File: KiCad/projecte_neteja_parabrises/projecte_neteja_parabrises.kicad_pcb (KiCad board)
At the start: 2 copper layers, 106.5 x 95.3 mm, 77 parts, among them J1 Conn_01x05_Pin, J2 DE9_Pins, J3 DE9_Pins, J4 Conn_01x02_Pin, K2 Fujitsu_FTR-LYAA005x, K3 Fujitsu_FTR-LYAA005x, K4 Fujitsu_FTR-LYAA005x, M1 Motor_DC, M2 Motor_DC, M3 Motor_DC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

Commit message: pcb
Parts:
- added TP1: TestPoint, TestPoint:TestPoint_Keystone_5015_Micro_Mini, F.Cu at (209.1, 109.7)
- added TP2: TestPoint, TestPoint:TestPoint_Keystone_5015_Micro_Mini, F.Cu at (209.1, 114.0)
- added TP3: TestPoint, TestPoint:TestPoint_Keystone_5015_Micro_Mini, F.Cu at (209.1, 118.3)
- moved C2 9.76 mm to (143.9, 101.7)
- moved C3 9.32 mm to (149.5, 96.2)
- moved C4 9.32 mm to (149.5, 92.5)
- moved Y1 7.62 mm to (143.0, 93.4)
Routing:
- net OSC1: track 0.00 -> 11.2 mm
- net OSC2: track 0.00 -> 10.2 mm

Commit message: pcb
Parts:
- removed BT1: 12V, TerminalBlock:TerminalBlock_MaiXu_MX126-5.0-02P_1x02_P5.00mm
- added REF**: MountingHole_2.2mm_M2_DIN965_Pad, MountingHole:MountingHole_2.2mm_M2_DIN965_Pad, F.Cu at (88.4, 56.8)
- added REF**: MountingHole_2.2mm_M2_DIN965_Pad, MountingHole:MountingHole_2.2mm_M2_DIN965_Pad, F.Cu at (87.6, 148.6)
- added REF**: MountingHole_2.2mm_M2_DIN965_Pad, MountingHole:MountingHole_2.2mm_M2_DIN965_Pad, F.Cu at (190.0, 56.8)
- added REF**: MountingHole_2.2mm_M2_DIN965_Pad, MountingHole:MountingHole_2.2mm_M2_DIN965_Pad, F.Cu at (191.4, 148.8)
- SW3: value CALEFACTOR -> SW
- moved C15 118.5 mm to (102.9, 36.9)
- moved D2 116.1 mm to (104.7, 41.4), turned to 90 degrees
- moved R8 115.7 mm to (100.9, 41.4)
- moved C14 101.6 mm to (140.8, 59.0), turned to 180 degrees
- moved C11 95.9 mm to (69.2, 93.8), turned to 180 degrees
- moved U2 89.0 mm to (107.3, 68.2), turned to 180 degrees
- moved SW3 86.6 mm to (34.0, 71.8)
- moved R2 84.8 mm to (23.8, 99.7)
- moved R3 84.8 mm to (23.0, 81.1)
- moved R7 84.8 mm to (26.6, 75.2)
- moved R6 80.4 mm to (145.7, 60.0), turned to -90 degrees
- moved U1 79.8 mm to (138.4, 70.6)
- moved R5 78.4 mm to (148.3, 60.0), turned to 90 degrees
- moved D3 77.0 mm to (124.1, 70.4), turned to 0 degrees
- moved C13 76.5 mm to (167.5, 63.2)
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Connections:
- C11 pad 1: Vbat -> 12V
- J4 pad 1: Vbat -> 12V
- TP1 pad 1: Vbat -> 12V
- U2 pad 1: Vbat -> 12V
- U4 pad 13: unconnected-(U4-RA7-Pad13) -> GATE C
- U4 pad 14: GATE C -> GATE B2
- U4 pad 19: GATE B2 -> unconnected-(U4-RA0-Pad19)
- U4 pad 23: RX -> TX
- U4 pad 24: TX -> RX
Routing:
- net TX: track 0.00 -> 44.4 mm
- net PWM2: track 0.00 -> 44.2 mm, vias 0 -> 2
- net RX: track 0.00 -> 44.2 mm
- net PWM: track 0.00 -> 36.3 mm, vias 0 -> 2
- net SW1: track 0.00 -> 32.6 mm, vias 0 -> 1
- net CANTX: track 0.00 -> 31.9 mm
- net CANRX: track 0.00 -> 31.3 mm
- net GATE B: track 0.00 -> 28.9 mm, vias 0 -> 2
- net SW3: track 0.00 -> 23.4 mm, vias 0 -> 2
- net Net-(U8-CANH): track 0.00 -> 22.1 mm
- net SW2: track 0.00 -> 21.7 mm, vias 0 -> 2
- net Net-(U9-T1OUT): track 0.00 -> 20.8 mm, vias 0 -> 2
- net Net-(C2-Pad2): track 0.00 -> 18.7 mm
- net Net-(U8-CANL): track 0.00 -> 18.7 mm
- net Net-(U9-R1IN): track 0.00 -> 16.4 mm
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- added copper zone on F.Cu, net 12V
- added copper zone on F.Cu, net 5V
- added copper zone on B.Cu, net GND
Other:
- board size 106.5 x 95.3 mm -> 109.7 x 98.2 mm

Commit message: pcb
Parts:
- moved R3 135.0 mm to (157.9, 76.1)
- moved FINALCARRERA2 130.0 mm to (161.8, 71.9), turned to 0 degrees
- moved R2 118.3 mm to (138.9, 72.5)
- moved C11 113.5 mm to (176.8, 130.1), turned to -90 degrees
- moved R7 110.4 mm to (133.4, 103.0), turned to 0 degrees
- moved SW3 109.0 mm to (137.8, 105.1), turned to -90 degrees
- moved C15 86.8 mm to (136.6, 117.0)
- moved D2 85.4 mm to (143.6, 117.5), turned to 180 degrees
- moved R8 84.8 mm to (143.6, 114.7), turned to 0 degrees
- moved FINALCARRERA1 79.4 mm to (142.7, 72.1), turned to 0 degrees
- moved R19 63.4 mm to (104.9, 112.2), turned to 0 degrees
- moved SW5 61.8 mm to (103.5, 109.7), turned to 90 degrees
- moved C16 57.2 mm to (114.8, 61.0), turned to -90 degrees
- moved C13 56.7 mm to (110.8, 61.0), turned to 180 degrees
- moved C1 54.4 mm to (128.8, 101.9), turned to -90 degrees
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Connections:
- R2 pad 1: VCC -> VDD
- R3 pad 1: VCC -> VDD
- U4 pad 11: unconnected-(U4-RB13-Pad11) -> SW1
- U4 pad 3: FC2 -> SW3
- U4 pad 33: unconnected-(U4-RB4-Pad33) -> FC2
- U4 pad 34: unconnected-(U4-RA4-Pad34) -> FC1
- U4 pad 35: SW1 -> unconnected-(U4-RA9-Pad35)
- U4 pad 36: SW2 -> unconnected-(U4-RP19-Pad36)
- U4 pad 37: SW3 -> unconnected-(U4-RP20-Pad37)
- U4 pad 4: FC1 -> SW2
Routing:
- net FC2: track 0.00 -> 55.9 mm, vias 0 -> 1
- net Net-(J1-Pin_1): track 0.00 -> 44.8 mm, vias 0 -> 4
- net GATE B2: track 4.02 -> 43.0 mm, vias 1 -> 2
- net FC1: track 0.00 -> 38.3 mm, vias 0 -> 1
- net PGD: track 0.00 -> 37.1 mm, vias 0 -> 2
- net PGC: track 0.00 -> 36.2 mm, vias 0 -> 2
- net GATE C: track 0.00 -> 35.1 mm, vias 0 -> 2
- net Net-(U4-VCAP): track 0.00 -> 12.4 mm
- net SW2: track 21.7 -> 33.5 mm, vias 2 -> 1
- net SW3: track 23.4 -> 30.8 mm, vias 2 -> 1
- net Net-(U4-AVdd): track 0.00 -> 4.50 mm
- net Net-(K3-Pad14): track 7.50 -> 11.8 mm
- net Net-(R7-Pad2): track 7.58 -> 3.55 mm
- net Net-(JP1-B): track 0.00 -> 3.87 mm
- net Net-(D2-K): track 0.14 -> 2.83 mm
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- added copper zone on F.Cu, net VDD
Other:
- board size 109.7 x 98.2 mm -> 117.5 x 103.8 mm

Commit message: test points
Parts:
- moved TP1 128.9 mm to (86.1, 71.1)
- moved TP2 126.1 mm to (95.0, 60.2)
- moved TP3 90.1 mm to (131.5, 72.5)
- moved FB1 5.50 mm to (120.6, 123.6), turned to 90 degrees
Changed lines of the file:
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@@
 	(footprint "TestPoint:TestPoint_Keystone_5015_Micro_Mini"
 		(layer "F.Cu")
-		(at 209.1 118.35)
+		(at 131.5 72.5)
 		(descr "Keystone SMT Micro Mini Test Point 5015, http://www.keyelco.com/product-pdf.cfm?p=1353")
 		(tags "Test Point")
@@
 	(footprint "TestPoint:TestPoint_Keystone_5015_Micro_Mini"
 		(layer "F.Cu")
-		(at 209.1 114)
+		(at 95 60.2)
 		(descr "Keystone SMT Micro Mini Test Point 5015, http://www.keyelco.com/product-pdf.cfm?p=1353")
 		(tags "Test Point")
@@
 	(footprint "Ferrite_THT:LairdTech_28C0236-0JW-10"
 		(layer "F.Cu")
-		(at 118.52 118.55)
+		(at 120.6 123.64 90)
 		(descr "Ferrite, vertical, LairdTech 28C0236-0JW-10, https://assets.lairdtech.com/home/brandworld/files/28C0236-0JW-10.pdf, JW Miller core https://www.bourns.com/products/magnetic-products/j.w.-miller-through-hole-ferrite-beads-emi-filters")
 		(tags "Ferrite vertical LairdTech 28C0236-0JW-10")
 		(property "Reference" "FB1"
-			(at 2.54 -4.064 0)
+			(at 2.54 -4.064 90)
 			(layer "F.SilkS")
 			(effects
@@
 		)
 		(property "Value" "FerriteBead"
-			(at 2.54 4.953 0)
+			(at 2.54 4.953 90)
 			(layer "F.Fab")
 			(effects
@@
 		)
 		(property "Datasheet" "~"
-			(at 0 0 0)
+			(at 0 0 90)
 			(unlocked yes)
 			(layer "F.Fab")
@@
 		)
 		(property "Description" "Ferrite bead"
-			(at 0 0 0)
+			(at 0 0 90)
 			(unlocked yes)
 			(layer "F.Fab")
@@
 		(attr through_hole)
 		(fp_arc
-			(start -0.508 1.27)
-			(mid -1.367832 0)
-			(end -0.508 -1.27)
+			(start 0.239932 -2.300068)
+			(mid 2.71988 -3.24781)
+			(end 5.08 -2.032)
 			(stroke
 				(width 0.12)
@@
 		)
 		(fp_arc
-			(start 0.239932 -2.300068)
-			(mid 2.71988 -3.24781)
-			(end 5.08 -2.032)
+			(start 5.588 -1.27)
+			(mid 6.447832 0)
+			(end 5.588 1.27)
 			(stroke
 				(width 0.12)
@@
 		)
 		(fp_arc
-			(start 5.064465 2.019572)
-			(mid 2.71878 3.227946)
-			(end 0.254 2.286)
+			(start -0.508 1.27)
+			(mid -1.367832 0)
+			(end -0.508 -1.27)
 			(stroke
 				(width 0.12)
@@
 		)
 		(fp_arc
-			(start 5.588 -1.27)
-			(mid 6.447832 0)
-			(end 5.588 1.27)
+			(start 5.064465 2.019572)
+			(mid 2.71878 3.227946)
+			(end 0.254 2.286)
 			(stroke
 				(width 0.12)
@@
 		)
 		(fp_arc
-			(start 0 1.145)
-			(mid -1.145 0)
-			(end 0 -1.145)
+			(start 5.08 -1.145)
+			(mid 6.225 0)
+			(end 5.08 1.145)
 			(stroke
 				(width 0.1)
@@
 		)
 		(fp_arc
-			(start 5.08 -1.145)
-			(mid 6.225 0)
-			(end 5.08 1.145)
+			(start 0 1.145)
+			(mid -1.145 0)
+			(end 0 -1.145)
 			(stroke
 				(width 0.1)
@@
 		)
 		(fp_text user "${REFERENCE}"
-			(at 2.54 0 0)
+			(at 2.54 0 90)
 			(layer "F.Fab")
 			(effects
@@
 		)
 		(pad "1" thru_hole circle
-			(at 0 0)
+			(at 0 0 90)
 			(size 2 2)
 			(drill 0.8)
@@
 		)
 		(pad "2" thru_hole circle
-			(at 5.08 0)
+			(at 5.08 0 90)
 			(size 2 2)
 			(drill 0.8)
@@
 	(footprint "TestPoint:TestPoint_Keystone_5015_Micro_Mini"
 		(layer "F.Cu")
-		(at 209.1 109.65)
+		(at 86.1 71.1)
 		(descr "Keystone SMT Micro Mini Test Point 5015, http://www.keyelco.com/product-pdf.cfm?p=1353")
 		(tags "Test Point")
@@
 	)
 	(segment
+		(start 125.77 72.5)
+		(end 125.62 72.65)
+		(width 0.25)
+		(layer "F.Cu")
+		(net 13)
+	)
+	(segment
 		(start 129.0504 90.0641)
 		(end 129.0504 89.0996)
@@
 		(polygon
 			(pts
-				(xy 77.25 54.175) (xy 77.5 68.8) (xy 160.35 68.35) (xy 160.25 86.9) (xy 160.25 86.9) (xy 160.1125 120.75)
-				(xy 193.3 120.4) (xy 193.625 53.875)
+				(xy 77.25 54.175) (xy 77.5 68.8) (xy 160.35 68.35) (xy 160.25 86.9) (xy 160.1125 120.75) (xy 193.3 120.4)
+				(xy 193.625 53.875)
 			)
 		)

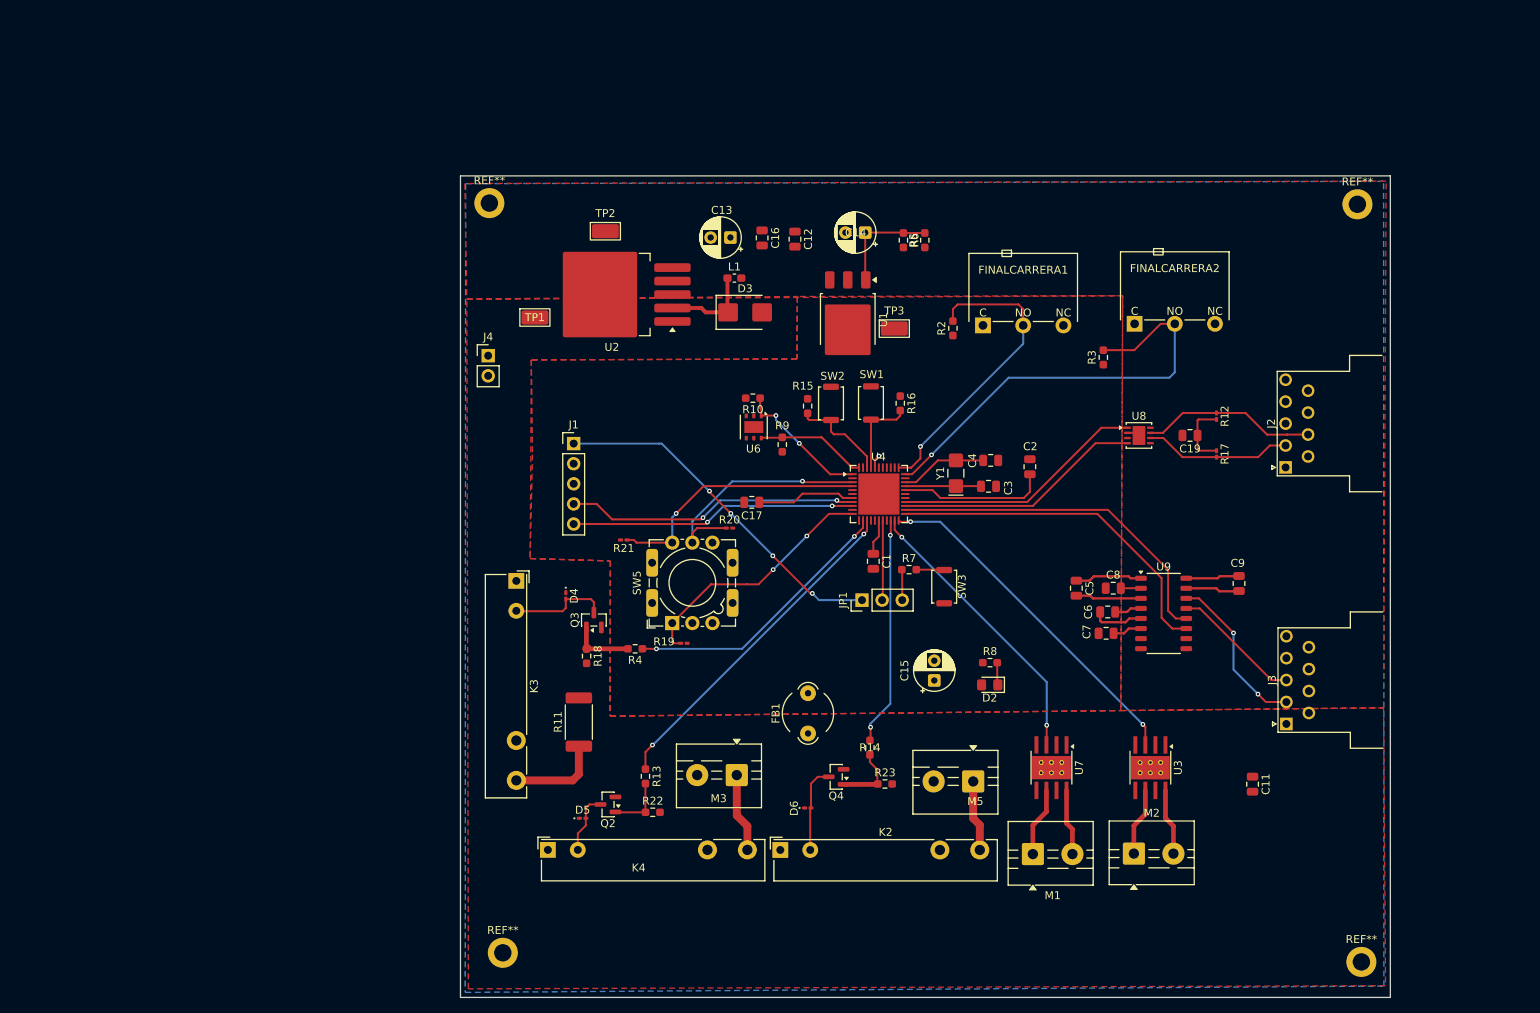
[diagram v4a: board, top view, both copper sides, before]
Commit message: actualitzacio pcb
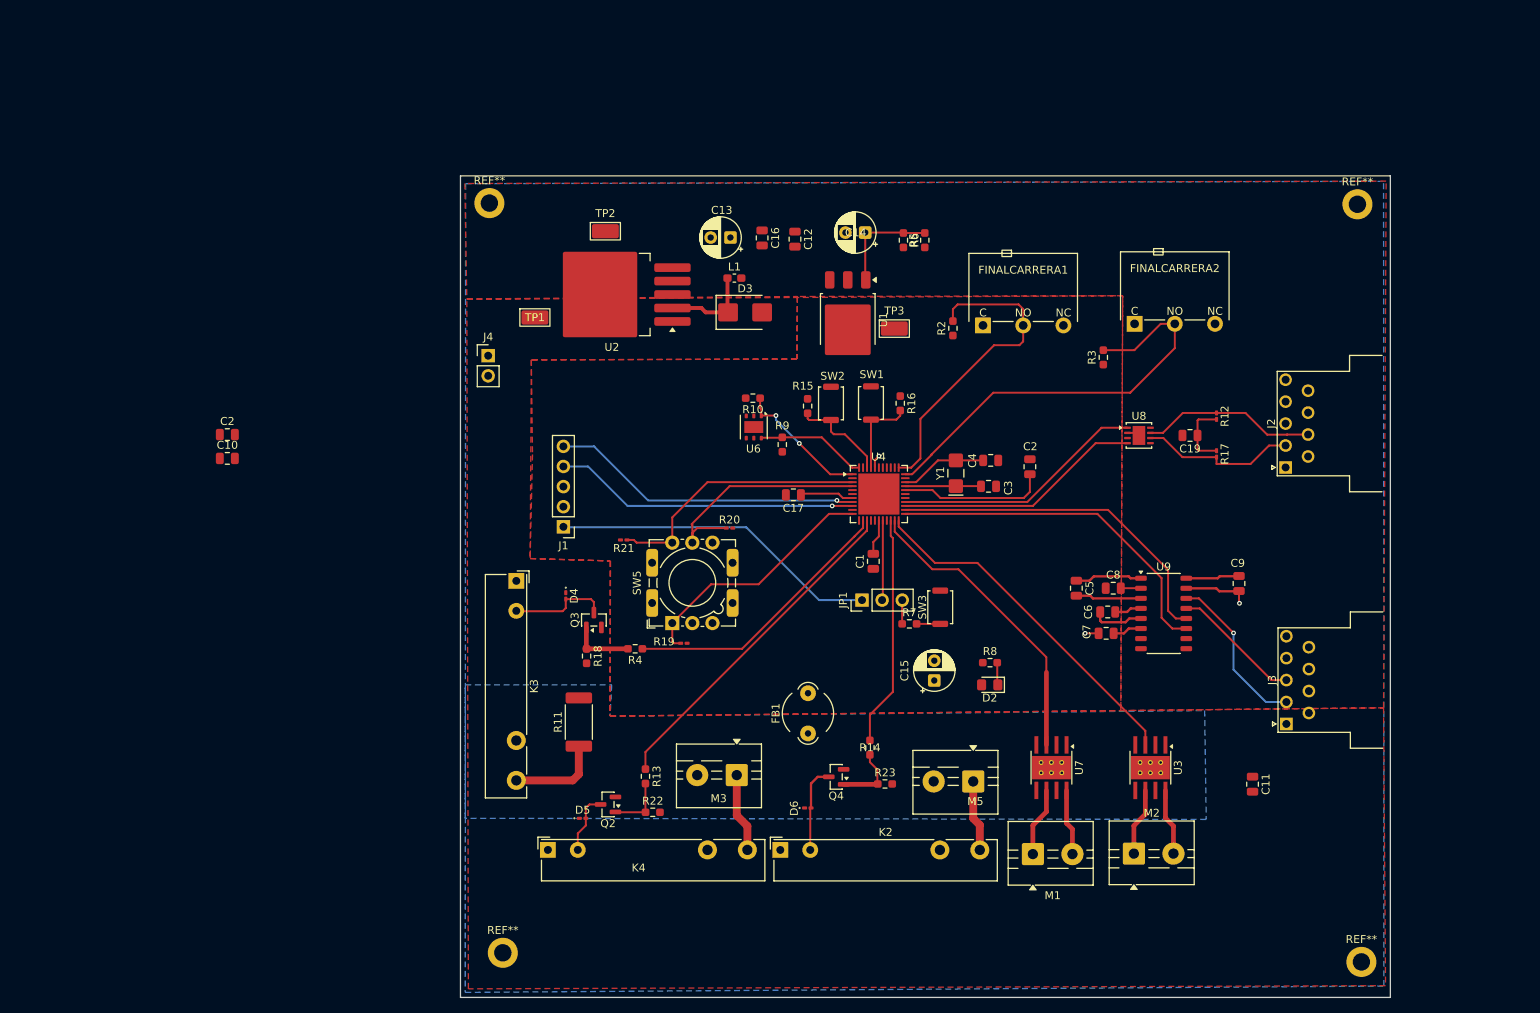
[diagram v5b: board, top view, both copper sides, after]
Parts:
- added C10: 100n, Capacitor_SMD:C_0805_2012Metric, F.Cu at (47.2, 88.9)
- added C2: 100n, Capacitor_SMD:C_0805_2012Metric, F.Cu at (47.2, 85.9)
- moved J1 10.6 mm to (89.7, 97.5), turned to 180 degrees
- moved R7 6.85 mm to (133.4, 109.8)
- moved C17 5.34 mm to (118.8, 93.5)
- moved SW3 2.65 mm to (137.3, 107.7), turned to 90 degrees
- turned C1 to 90 degrees
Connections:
- C1 pad 1: Net-(U4-AVdd) -> GND
- C1 pad 2: GND -> VDD
- U4 pad 17: Net-(U4-AVdd) -> VDD
- U4 pad 29: Net-(C2-Pad2) -> GND
- U4 pad 3: SW3 -> SW2
- U4 pad 39: unconnected-(U4-Vss-Pad39) -> GND
- U4 pad 4: SW2 -> SW3
- U4 pad 8: PGD -> PGC
- U4 pad 9: PGC -> PGD
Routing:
- net Net-(U4-VCAP): track 12.4 -> 6.54 mm
- net VDD: track 1.88 -> 6.38 mm
- net Net-(U4-AVdd): track 4.50 -> 0.00 mm
- net PGC: track 36.2 -> 39.4 mm, vias 2 -> 1
- net Net-(J1-Pin_1): track 44.8 -> 41.6 mm, vias 4 -> 0
- net GND: track 7.94 -> 11.1 mm, vias 0 -> 2
- net FC1: track 38.3 -> 40.2 mm, vias 1 -> 0
- net PWM: track 36.3 -> 38.2 mm, vias 2 -> 0
- net FC2: track 55.9 -> 54.1 mm, vias 1 -> 0
- net PGD: track 37.1 -> 38.6 mm, vias 2 -> 1
- net Net-(U8-CANL): track 18.7 -> 19.9 mm
- net GND_PWR: track 0.97 -> 0.00 mm
- net Net-(JP1-B): track 3.87 -> 3.01 mm
- net Net-(R7-Pad2): track 3.55 -> 2.99 mm
- net SW3: track 30.8 -> 30.4 mm, vias 1 -> 0
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- added copper zone on B.Cu, net GND_PWR

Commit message: pcb cristal
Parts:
- moved C2 93.5 mm to (139.7, 99.5), turned to 90 degrees
- moved C10 84.6 mm to (131.8, 86.6), turned to 180 degrees
- moved REF** 6.76 mm to (189.6, 145.8)
- moved REF** 5.41 mm to (80.5, 146.2)
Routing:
- net VDD: track 6.38 -> 9.60 mm, vias 1 -> 0
- net TX: track 44.4 -> 46.4 mm
- net RX: track 44.2 -> 46.0 mm
- net GND: track 11.1 -> 10.4 mm
- added copper zone on F.Cu, net GND
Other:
- board size 117.5 x 103.8 mm -> 117.2 x 96.5 mm

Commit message: vias pcb
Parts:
- removed the C2 at (148.6, 90.0)
- JP1: value Jumper_3_Bridged12 -> Jumper_3_Bridged
- moved R5 7.85 mm to (130.3, 67.3)
- moved R23 4.22 mm to (129.3, 134.1), turned to -90 degrees
- moved FB1 2.79 mm to (121.0, 126.4)
- moved R11 2.12 mm to (90.9, 124.2), turned to 180 degrees
- moved R20 1.97 mm to (111.9, 96.2)
- moved D5 0.90 mm to (92.0, 133.5)
- moved C12 0.20 mm to (119.0, 61.0)
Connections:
- U6 pad 5: VDD -> 5V
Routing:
- net GND: track 10.4 -> 79.0 mm, vias 2 -> 31
- net Net-(C2-Pad2): track 18.7 -> 0.00 mm
- net VDD: track 9.60 -> 20.4 mm
- net Net-(Q4-B): track 8.45 -> 14.5 mm
- net GATE C: track 35.1 -> 38.5 mm
- net SW3: track 30.4 -> 33.2 mm
- net Net-(K3-Pad14): track 11.8 -> 13.8 mm
- net GND_PWR: track 0.00 -> 0.91 mm, vias 0 -> 2

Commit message: pcb
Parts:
- moved U6 16.8 mm to (116.0, 68.3), turned to 90 degrees
- moved R9 10.8 mm to (110.9, 78.5), turned to 0 degrees
- moved D3 5.93 mm to (106.8, 69.5)
- moved L1 5.93 mm to (105.5, 65.1)
- moved D5 5.87 mm to (97.8, 132.2), turned to -90 degrees
- moved TP1 5.79 mm to (80.3, 71.0)
- moved R10 4.56 mm to (115.8, 77.3), turned to 0 degrees
- moved TP2 4.30 mm to (90.7, 59.7)
- moved U2 4.30 mm to (91.6, 67.7)
- moved C13 3.58 mm to (108.0, 58.8)
- moved C19 1.94 mm to (170.8, 85.9), turned to 0 degrees
- moved Q2 1.67 mm to (96.2, 134.0), turned to 0 degrees
- moved U8 1.45 mm to (163.8, 86.2)
- moved R20 1.23 mm to (113.1, 96.2)
- moved C4 1.14 mm to (142.6, 89.4)
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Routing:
- net SCL: track 13.5 -> 35.8 mm, vias 0 -> 2
- net GND_PWR: track 0.91 -> 15.8 mm, vias 2 -> 1
- net SDA: track 17.6 -> 31.3 mm, vias 2 -> 0
- net GND: track 79.0 -> 89.0 mm, vias 31 -> 39
- net Net-(Q2-B): track 7.38 -> 11.0 mm
- net CANTX: track 31.9 -> 34.5 mm
- net Net-(D5-A): track 7.80 -> 10.3 mm
- net 5V: track 6.17 -> 8.58 mm, vias 0 -> 2
- net CANRX: track 31.3 -> 33.1 mm
- net Net-(D3-A1): track 11.5 -> 9.84 mm
- net Net-(U8-CANL): track 19.9 -> 18.4 mm
- net Net-(U8-CANH): track 22.1 -> 20.7 mm
- net SW3: track 33.2 -> 34.5 mm
- net OSC2: track 11.0 -> 9.76 mm
- net VDD: track 20.4 -> 21.3 mm, vias 0 -> 1
